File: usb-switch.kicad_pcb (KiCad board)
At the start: 6 copper layers, 119.8 x 50 mm, 53 parts, among them IC1 MAX20337AEFT+T, IC2 MAX20337AEFT+T, IC3 MAX20337AEFT+T, IC4 MAX20337AEFT+T, IC5 TS3USB221ERSER, IC6 ESP32-S3-WROOM-1-N8R8, J1 DX07P024AJ1R1500, J2 Conn_01x05_Pin, J3 Conn_01x05_Pin, J5 Conn_01x06_Pin, J6 USB_C_Receptacle_USB2.0_16P, Q1 SIR5607DP-T1-RE3, Q2 SSM3K7002KFU,LF, Q3 SSM3K7002KFU,LF, Q4 SIR5607DP-T1-RE3, Q5 SSM3K7002KFU,LF, Q6 SSM3K7002KFU,LF, Q7 SIR5607DP-T1-RE3, Q8 SIR5607DP-T1-RE3, SW2 SW, SW3 SW, U1 74LVC1GU04DRL, U2 74LVC1GU04DRL, U3 DX07S024XJ1R1100, U4 DX07S024XJ1R1100, U5 AMS1117-3.3

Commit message: add capacitors, move B pwr control, select remaining components
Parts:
- added C1: 0.1u, Capacitor_SMD:C_0402_1005Metric, F.Cu at (125.3, 88.0)
- added C2: 0.1u, Capacitor_SMD:C_0402_1005Metric, B.Cu at (130.2, 52.2)
- added C3: 10u, Capacitor_SMD:C_0402_1005Metric, F.Cu at (130.8, 63.5)
- added C4: 10u, Capacitor_SMD:C_0402_1005Metric, F.Cu at (130.8, 57.5)
- added C5: 10u, Capacitor_SMD:C_0402_1005Metric, F.Cu at (130.8, 60.5)
- added C6: 10u, Capacitor_SMD:C_0402_1005Metric, F.Cu at (130.8, 66.5)
- added C7: 10u, Capacitor_SMD:C_0402_1005Metric, F.Cu at (127.8, 81.7)
- added C8: 10u, Capacitor_SMD:C_0402_1005Metric, F.Cu at (128.9, 69.4)
- added R7: 330R, Resistor_SMD:R_0402_1005Metric, F.Cu at (206.9, 79.8)
- added R9: 330R, Resistor_SMD:R_0402_1005Metric, F.Cu at (206.9, 78.5)
- D1, D2: value D_Zener -> MM3Z10VST1G; footprint Diode_SMD:D_0402_1005Metric -> Diode_SMD:D_SOD-323
- moved R3 5.19 mm to (117.2, 60.4), turned to 180 degrees
- moved D1 5.07 mm to (117.2, 58.9), turned to 180 degrees
- moved Q2 2.20 mm to (123.3, 63.5)
- moved R1 2.09 mm to (122.2, 58.5), turned to 0 degrees
- moved Q1 1.85 mm to (123.3, 60.5)
- moved U2 0.71 mm to (132.1, 53.2)
- moved D2 0.59 mm to (117.2, 91.1)
- moved R4 0.56 mm to (117.2, 89.7)
- moved Q5 0.40 mm to (134.6, 94.7)
- moved R2 0.21 mm to (128.3, 91.1)
- renumbered C2 to C10, C3 to C11, C4 to C12, C5 to C13, C6 to C14, C1 to C9, J6 to J4, Q2 to Q1, Q3 to Q2, Q1 to Q3, Q5 to Q4, Q6 to Q5, Q4 to Q6, R6 to R10, R7 to R11, R8 to R12, R9 to R5, R10 to R6, R5 to R8
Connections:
- C11 pad 1: Net-(IC6-IO18) -> Net-(C11-Pad1)
- C14 pad 1: Net-(IC6-IO8) -> Net-(C14-Pad1)
- R10 pad 2: Net-(IC6-IO8) -> Net-(C14-Pad1)
- R8 pad 2: Net-(IC6-IO18) -> Net-(C11-Pad1)
- SW1 pad 11: /COM_TX1- -> /COM_RX1-
- SW1 pad 12: /COM_TX1+ -> /COM_RX1+
- SW1 pad 15: /COM_RX1- -> /COM_TX1-
- SW1 pad 16: /COM_RX1+ -> /COM_TX1+
- SW2 pad 2: Net-(IC6-IO18) -> Net-(C11-Pad1)
- SW3 pad 2: Net-(IC6-IO8) -> Net-(C14-Pad1)
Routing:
- net Net-(IC6-IO8): track 22.1 -> 2.85 mm
- net Net-(C14-Pad1): track 0.00 -> 18.8 mm
- net Net-(IC6-IO18): track 15.4 -> 2.85 mm
- net Net-(C11-Pad1): track 0.00 -> 11.5 mm
- net /3v3: track 49.5 -> 57.3 mm, vias 8 -> 7
- net /GND: track 33.5 -> 40.5 mm, vias 31 -> 34
- net /EN: track 72.1 -> 77.3 mm
- net /PWR MUX/B_PWR_S: track 20.4 -> 17.9 mm
- net /PWR MUX/A_PWR_S: track 19.8 -> 18.0 mm
- net Net-(Q1-D): track 3.79 -> 2.17 mm
- net /SEL: track 81.3 -> 80.4 mm
- net /PWR MUX/B_PWR_G: track 20.6 -> 19.9 mm
- added copper zone on F.Cu, net /VBUS
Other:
- board text added: "USB4 Thing v0.1 by github.com/cubicap"

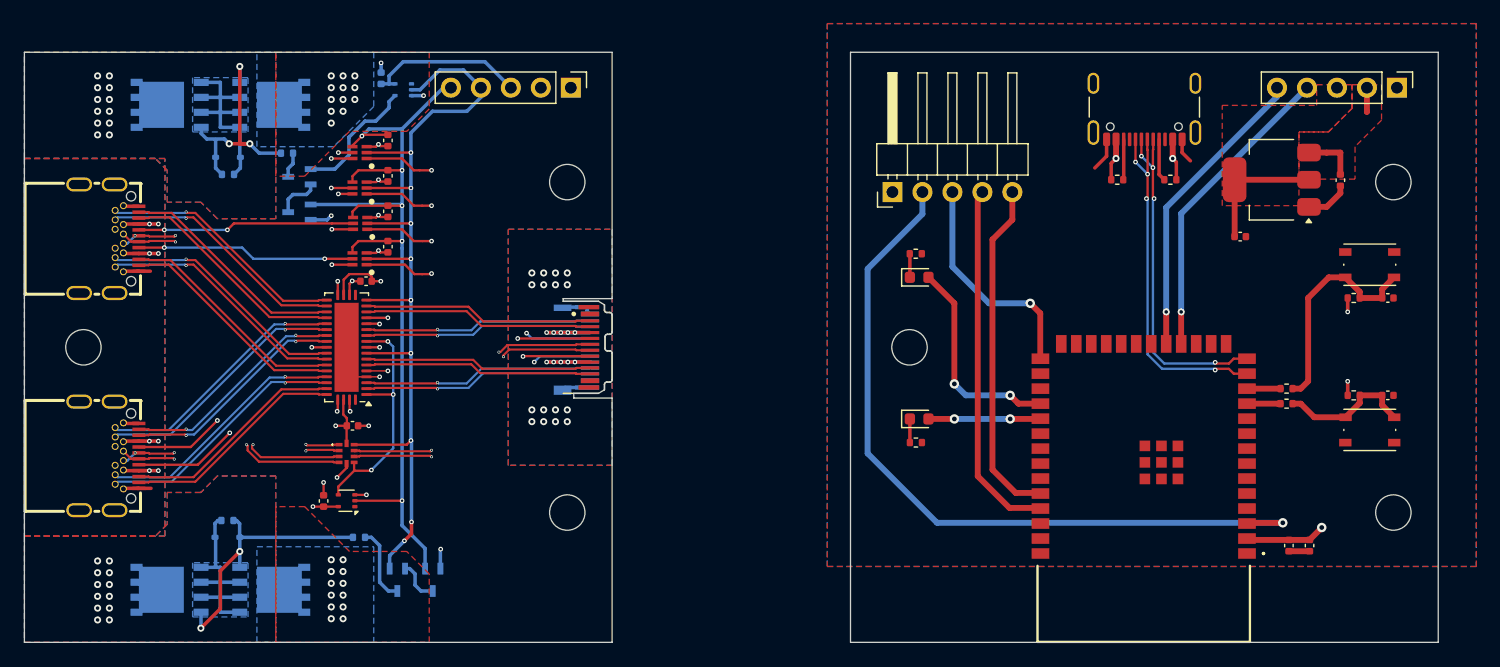
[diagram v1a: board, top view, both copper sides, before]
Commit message: fix usb connections, board dimensions
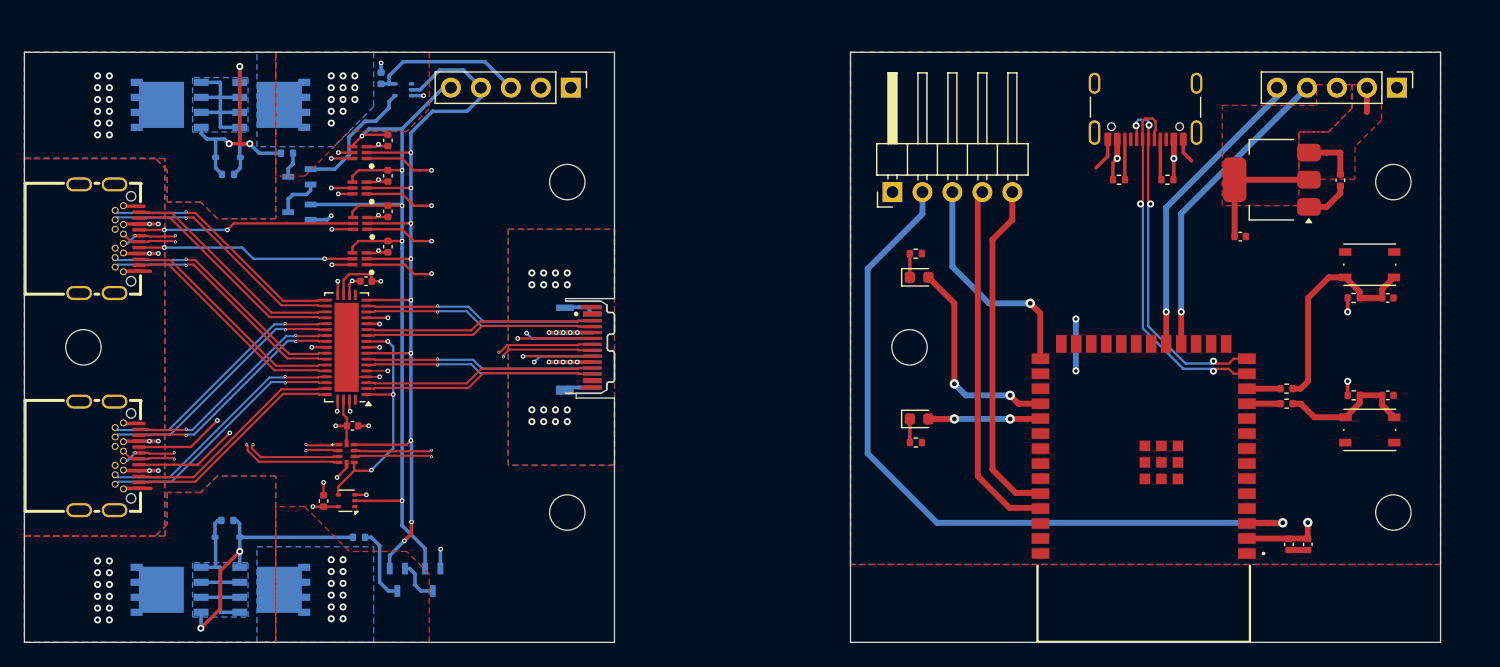
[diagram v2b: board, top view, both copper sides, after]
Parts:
- IC6: renamed from SW1; value ~ -> PI3DBS16412ZHEX
- moved R5 0.25 mm to (196.8, 60.8)
- moved J1 0.20 mm to (150.0, 75.0)
- moved C13 0.18 mm to (208.8, 91.7)
- moved R6 0.15 mm to (192.8, 60.8)
- moved J4 0.10 mm to (195.0, 53.7)
- moved C12 0.10 mm to (207.1, 91.7)
- renumbered IC6 to IC7, R3 to R2, R2 to R3, SW2 to SW1, SW3 to SW2
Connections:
- IC6 pad 11: /COM_RX1- -> /COM_TX1-
- IC6 pad 12: /COM_RX1+ -> /COM_TX1+
- IC6 pad 15: /COM_TX1- -> /COM_RX1-
- IC6 pad 16: /COM_TX1+ -> /COM_RX1+
- IC6 pad 2: /COM_TX2+ -> /COM_RX2+
- IC6 pad 3: /COM_TX2- -> /COM_RX2-
- IC6 pad 6: /COM_RX2+ -> /COM_TX2+
- IC6 pad 7: /COM_RX2- -> /COM_TX2-
- J4 pad A6: /control_board/D- -> /control_board/D+
- J4 pad A7: /control_board/D+ -> /control_board/D-
- J4 pad B6: /control_board/D- -> /control_board/D+
- J4 pad B7: /control_board/D+ -> /control_board/D-
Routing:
- net /control_board/GND: track 10.5 -> 14.7 mm, vias 0 -> 2
- net /control_board/D+: track 29.6 -> 30.3 mm
- net /control_board/D-: track 30.9 -> 31.2 mm, vias 4 -> 2
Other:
- board size 119.8 x 50 mm -> 120 x 50 mm

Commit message: fixes
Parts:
- added R13: 330R, Resistor_SMD:R_0402_1005Metric, F.Cu at (198.0, 68.2)
- added R14: 330R, Resistor_SMD:R_0402_1005Metric, F.Cu at (196.8, 68.2)
- moved R7 0.95 mm to (207.9, 79.8)
- moved R9 0.95 mm to (207.9, 78.5)
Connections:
- IC7 pad 18: /control_board/EN -> Net-(IC7-IO10)
- IC7 pad 19: /control_board/SEL -> Net-(IC7-IO11)
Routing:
- net /GND: track 40.5 -> 59.7 mm
- net /control_board/SEL: track 25.6 -> 18.6 mm
- net /control_board/EN: track 26.1 -> 19.1 mm
- net Net-(IC7-IO10): track 0.00 -> 6.00 mm
- net Net-(IC7-IO11): track 0.00 -> 6.00 mm
- net Net-(IC7-IO8): track 2.85 -> 3.80 mm
- net Net-(IC7-IO18): track 2.85 -> 3.80 mm
- net Net-(C11-Pad1): track 11.5 -> 10.5 mm
- net /3v3: track 57.3 -> 58.0 mm
